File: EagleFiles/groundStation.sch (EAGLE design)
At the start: 23 parts, among them IC1 TP4056

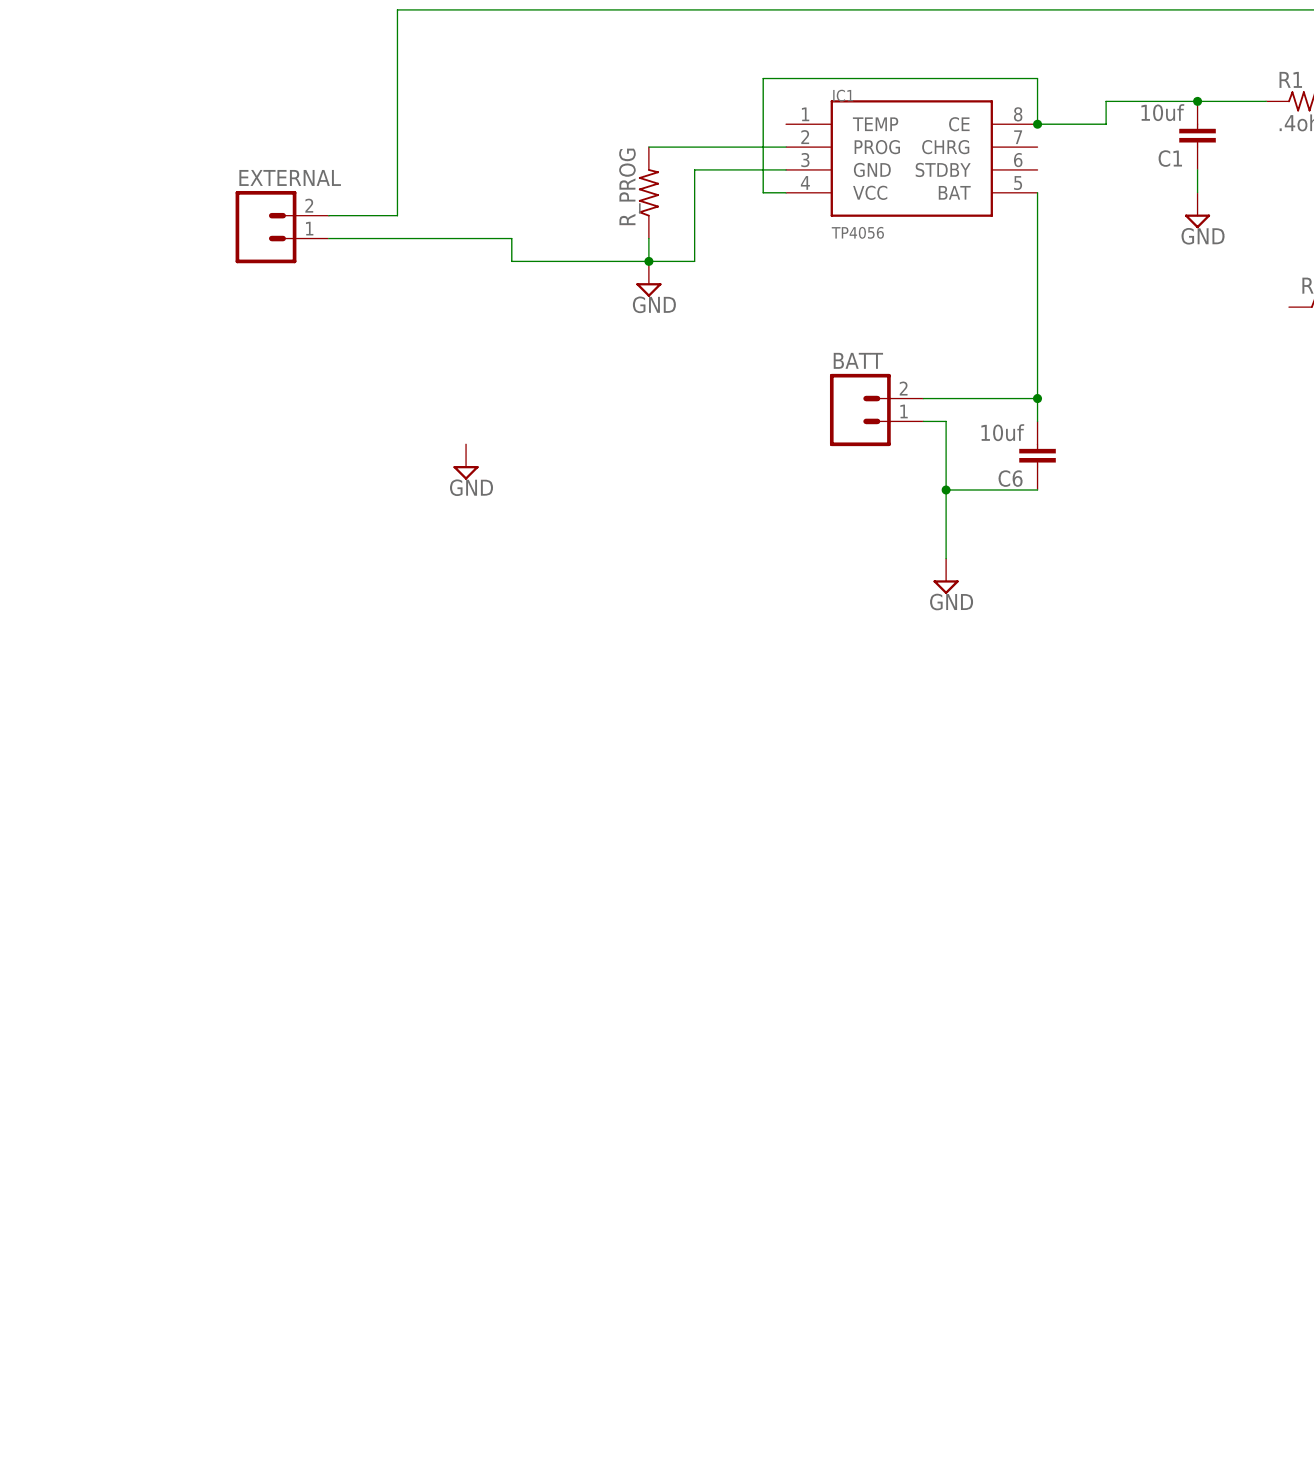
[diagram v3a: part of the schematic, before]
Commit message: added uass ground station
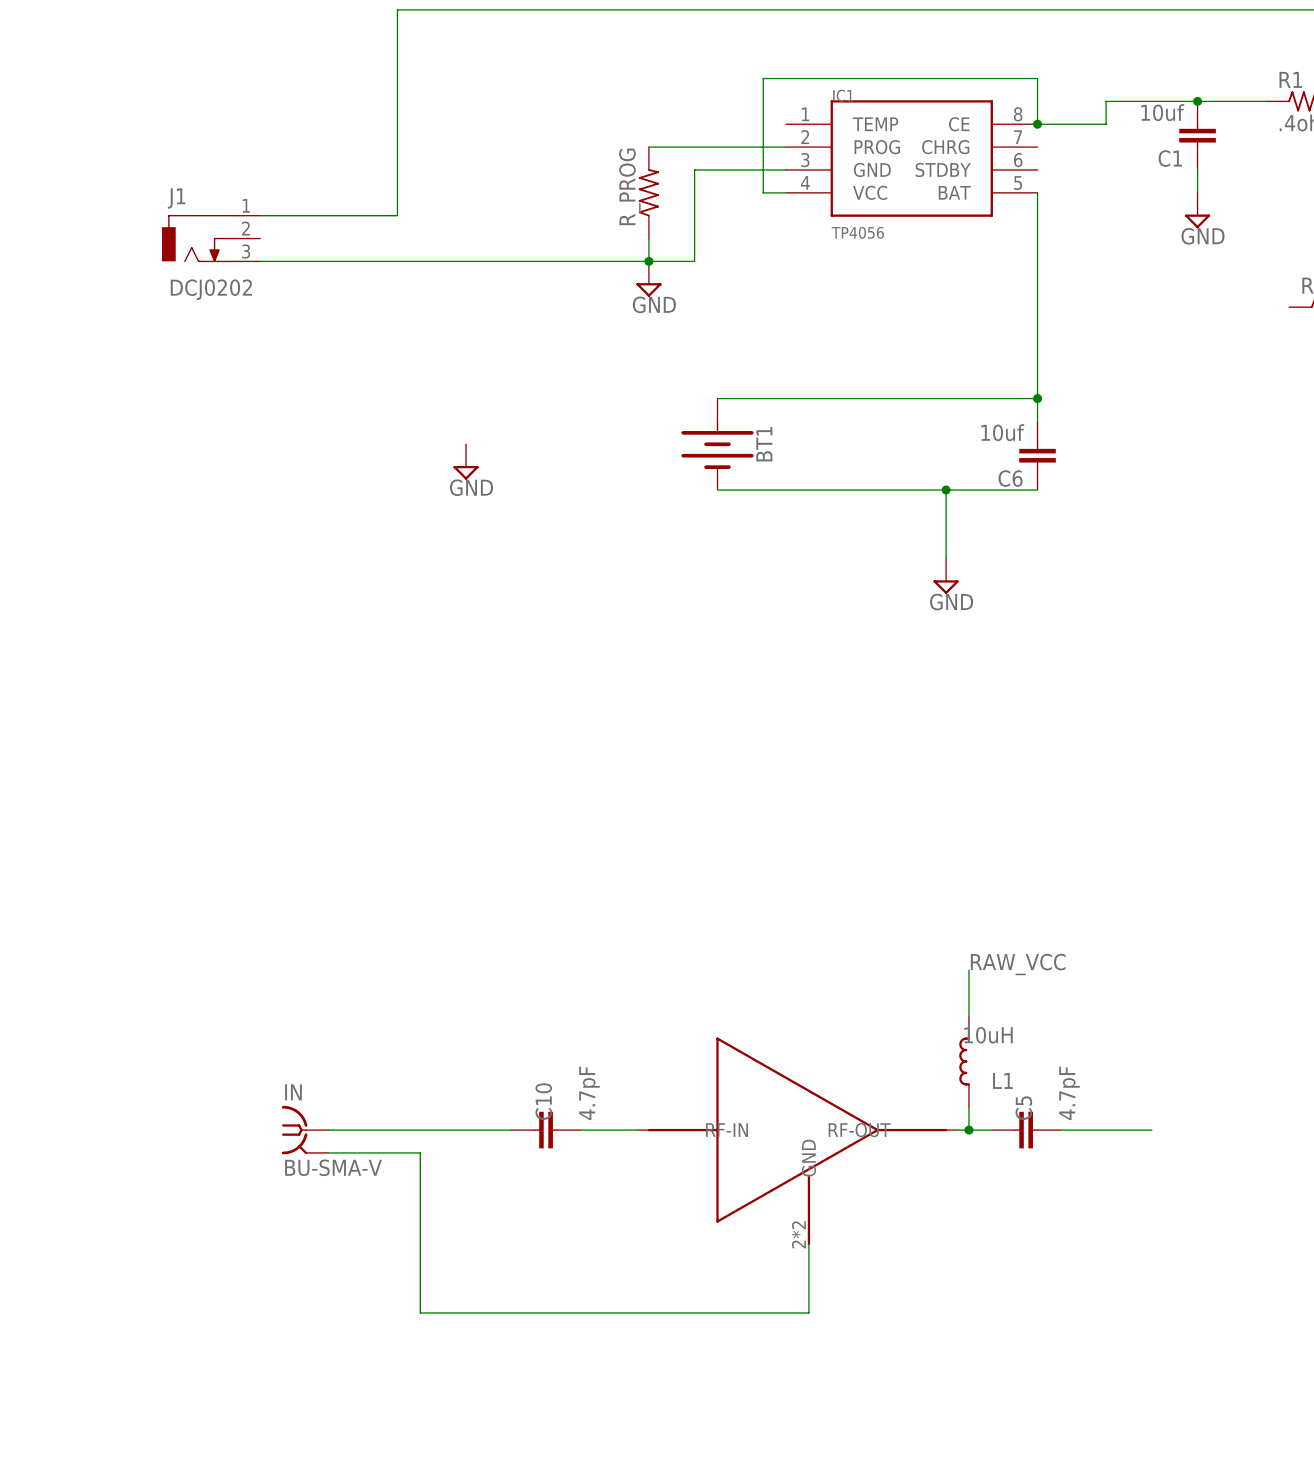
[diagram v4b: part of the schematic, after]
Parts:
- removed BATT, EXTERNAL: (no value), con-amp-quick:M02
- added BT1: (no value), SparkFun-Batteries:BATTERY-18650
- added C10, C5: 4.7pF, SparkFun-Capacitors:10UF-0603-6.3V-20%
- added IN: BU-SMA-V, con-coax:BU-SMA-V
- added J1: DCJ0202, con-jack:DCJ0202
- added L1: 10uH, rc-master-smd:L_0603
- added U$5: PSA4-5043+, PSA4-5043_:PSA4-5043+
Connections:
- new net GND3: IN.2, U$5.GND
- new net N$23: C5.2
- new net N$24: C10.1, IN.1
- new net N$25: C10.2, U$5.RF-IN
- new net N$26: C5.1, L1.2, U$5.RF-OUT
- net GND: now also BT1.-, J1.3; no longer BATT.1, EXTERNAL.1
- net N$1: now also BT1.+; no longer BATT.2
- net RAW_VCC: now also J1.1, L1.1; no longer EXTERNAL.2
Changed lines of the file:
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@@
 <part name="U$3" library="RFFM6406" deviceset="RFFM6404" device=""/>
 <part name="IC1" library="TP4056" deviceset="TP4056" device=""/>
-<part name="BATT" library="con-amp-quick" library_urn="urn:adsk.eagle:library:125" deviceset="M02" device="" package3d_urn="urn:adsk.eagle:package:5956/1"/>
 <part name="SUPPLY1" library="supply2" library_urn="urn:adsk.eagle:library:372" deviceset="GND" device=""/>
 <part name="R_PROG" library="adafruit" library_urn="urn:adsk.eagle:library:420" deviceset="R-US_" device="R0603" package3d_urn="urn:adsk.eagle:package:6240565/1"/>
@@
 <part name="C4" library="SparkFun-Capacitors" deviceset="0.1UF" device="-0603-100V-10%" value="1uf"/>
 <part name="R8" library="adafruit" library_urn="urn:adsk.eagle:library:420" deviceset="R-US_" device="R0603" package3d_urn="urn:adsk.eagle:package:6240565/1" value="50ohm"/>
-<part name="EXTERNAL" library="con-amp-quick" library_urn="urn:adsk.eagle:library:125" deviceset="M02" device="" package3d_urn="urn:adsk.eagle:package:5956/1"/>
+<part name="BT1" library="SparkFun-Batteries" library_urn="urn:adsk.eagle:library:508" deviceset="BATTERY" device="-18650" package3d_urn="urn:adsk.eagle:package:37227/1"/>
+<part name="J1" library="con-jack" library_urn="urn:adsk.eagle:library:154" deviceset="DCJ0202" device="" package3d_urn="urn:adsk.eagle:package:7491/1"/>
+<part name="U$5" library="PSA4-5043_" deviceset="PSA4-5043+" device=""/>
+<part name="C5" library="SparkFun-Capacitors" library_urn="urn:adsk.eagle:library:510" deviceset="10UF" device="-0603-6.3V-20%" package3d_urn="urn:adsk.eagle:package:37414/1" value="4.7pF"/>
+<part name="C10" library="SparkFun-Capacitors" library_urn="urn:adsk.eagle:library:510" deviceset="10UF" device="-0603-6.3V-20%" package3d_urn="urn:adsk.eagle:package:37414/1" value="4.7pF"/>
+<part name="L1" library="rc-master-smd" deviceset="L_" device="0603" value="10uH"/>
+<part name="IN" library="con-coax" library_urn="urn:adsk.eagle:library:133" deviceset="BU-SMA-V" device="" package3d_urn="urn:adsk.eagle:package:6211/1"/>
 </parts>
 <sheets>
@@
 <attribute name="VALUE" x="246.38" y="292.1" size="1.27" layer="96"/>
 </instance>
-<instance part="BATT" gate="G$1" x="248.92" y="271.78" smashed="yes">
-<attribute name="VALUE" x="246.38" y="266.7" size="1.778" layer="96"/>
-<attribute name="NAME" x="246.38" y="277.622" size="1.778" layer="95"/>
-</instance>
 <instance part="SUPPLY1" gate="GND" x="259.08" y="254" smashed="yes">
 <attribute name="VALUE" x="257.175" y="250.825" size="1.778" layer="96"/>
@@
 <attribute name="VALUE" x="46.482" y="242.57" size="1.778" layer="96" rot="R90"/>
 </instance>
-<instance part="EXTERNAL" gate="G$1" x="182.88" y="292.1" smashed="yes">
-<attribute name="VALUE" x="180.34" y="287.02" size="1.778" layer="96"/>
-<attribute name="NAME" x="180.34" y="297.942" size="1.778" layer="95"/>
+<instance part="BT1" gate="G$1" x="233.68" y="269.24" smashed="yes" rot="R270">
+<attribute name="NAME" x="237.998" y="269.24" size="1.778" layer="95" font="vector" rot="R270" align="bottom-center"/>
+<attribute name="VALUE" x="229.362" y="269.24" size="1.778" layer="96" font="vector" rot="R270" align="top-center"/>
+</instance>
+<instance part="J1" gate="G$1" x="175.26" y="292.1" smashed="yes">
+<attribute name="NAME" x="172.72" y="295.91" size="1.778" layer="95"/>
+<attribute name="VALUE" x="172.72" y="285.75" size="1.778" layer="96"/>
+</instance>
+<instance part="U$5" gate="G$1" x="241.3" y="193.04" smashed="yes"/>
+<instance part="C5" gate="G$1" x="269.24" y="193.04" smashed="yes" rot="R90">
+<attribute name="NAME" x="268.605" y="194.056" size="1.778" layer="95" rot="R90"/>
+<attribute name="VALUE" x="273.431" y="194.056" size="1.778" layer="96" rot="R90"/>
+</instance>
+<instance part="C10" gate="G$1" x="215.9" y="193.04" smashed="yes" rot="R90">
+<attribute name="NAME" x="215.265" y="194.056" size="1.778" layer="95" rot="R90"/>
+<attribute name="VALUE" x="220.091" y="194.056" size="1.778" layer="96" rot="R90"/>
+</instance>
+<instance part="L1" gate="G$1" x="261.62" y="200.66" smashed="yes" rot="R90">
+<attribute name="NAME" x="266.7" y="199.39" size="1.778" layer="95" rot="R180"/>
+<attribute name="VALUE" x="266.7" y="204.47" size="1.778" layer="96" rot="R180"/>
+</instance>
+<instance part="IN" gate="G$1" x="187.96" y="193.04" smashed="yes">
+<attribute name="VALUE" x="185.42" y="187.96" size="1.778" layer="96"/>
+<attribute name="NAME" x="185.42" y="196.342" size="1.778" layer="95"/>
 </instance>
 </instances>
@@
 </segment>
 <segment>
-<pinref part="BATT" gate="G$1" pin="1"/>
 <pinref part="SUPPLY1" gate="GND" pin="GND"/>
-<wire x1="256.54" y1="271.78" x2="259.08" y2="271.78" width="0.1524" layer="91"/>
-<wire x1="259.08" y1="271.78" x2="259.08" y2="264.16" width="0.1524" layer="91"/>
 <pinref part="C6" gate="G$1" pin="1"/>
 <wire x1="259.08" y1="264.16" x2="259.08" y2="256.54" width="0.1524" layer="91"/>
 <wire x1="269.24" y1="264.16" x2="259.08" y2="264.16" width="0.1524" layer="91"/>
+<pinref part="BT1" gate="G$1" pin="-"/>
+<wire x1="259.08" y1="264.16" x2="233.68" y2="264.16" width="0.1524" layer="91"/>
 <junction x="259.08" y="264.16"/>
 </segment>
@@
 <wire x1="231.14" y1="289.56" x2="226.06" y2="289.56" width="0.1524" layer="91"/>
 <junction x="226.06" y="289.56"/>
-<pinref part="EXTERNAL" gate="G$1" pin="1"/>
-<wire x1="190.5" y1="292.1" x2="210.82" y2="292.1" width="0.1524" layer="91"/>
-<wire x1="210.82" y1="292.1" x2="210.82" y2="289.56" width="0.1524" layer="91"/>
-<wire x1="210.82" y1="289.56" x2="226.06" y2="289.56" width="0.1524" layer="91"/>
+<pinref part="J1" gate="G$1" pin="3"/>
+<wire x1="226.06" y1="289.56" x2="182.88" y2="289.56" width="0.1524" layer="91"/>
 </segment>
 <segment>
@@
 <net name="N$1" class="0">
 <segment>
-<pinref part="BATT" gate="G$1" pin="2"/>
 <pinref part="IC1" gate="G$1" pin="BAT"/>
-<wire x1="256.54" y1="274.32" x2="269.24" y2="274.32" width="0.1524" layer="91"/>
+<wire x1="269.24" y1="271.78" x2="269.24" y2="274.32" width="0.1524" layer="91"/>
+<pinref part="C6" gate="G$1" pin="2"/>
+<pinref part="BT1" gate="G$1" pin="+"/>
 <wire x1="269.24" y1="274.32" x2="269.24" y2="297.18" width="0.1524" layer="91"/>
-<pinref part="C6" gate="G$1" pin="2"/>
-<wire x1="269.24" y1="271.78" x2="269.24" y2="274.32" width="0.1524" layer="91"/>
+<wire x1="233.68" y1="274.32" x2="269.24" y2="274.32" width="0.1524" layer="91"/>
 <junction x="269.24" y="274.32"/>
 </segment>
@@
 <wire x1="304.8" y1="307.34" x2="309.88" y2="307.34" width="0.1524" layer="91"/>
 <label x="309.88" y="307.34" size="1.778" layer="95"/>
-<pinref part="EXTERNAL" gate="G$1" pin="2"/>
-<wire x1="190.5" y1="294.64" x2="198.12" y2="294.64" width="0.1524" layer="91"/>
 <wire x1="198.12" y1="294.64" x2="198.12" y2="317.5" width="0.1524" layer="91"/>
 <wire x1="198.12" y1="317.5" x2="304.8" y2="317.5" width="0.1524" layer="91"/>
 <wire x1="304.8" y1="317.5" x2="304.8" y2="307.34" width="0.1524" layer="91"/>
 <junction x="304.8" y="307.34"/>
+<pinref part="J1" gate="G$1" pin="1"/>
+<wire x1="182.88" y1="294.64" x2="198.12" y2="294.64" width="0.1524" layer="91"/>
 </segment>
 <segment>
@@
 <wire x1="0" y1="35.56" x2="-15.24" y2="35.56" width="0.1524" layer="91"/>
 <label x="-12.7" y="35.56" size="1.778" layer="95"/>
+</segment>
+<segment>
+<pinref part="L1" gate="G$1" pin="1"/>
+<wire x1="261.62" y1="205.74" x2="261.62" y2="210.82" width="0.1524" layer="91"/>
+<label x="261.62" y="210.82" size="1.778" layer="95"/>
 </segment>
 </net>
@@
 </segment>
 </net>
+<net name="N$23" class="0">
+<segment>
+<pinref part="C5" gate="G$1" pin="2"/>
+<wire x1="271.78" y1="193.04" x2="281.94" y2="193.04" width="0.1524" layer="91"/>
+</segment>
+</net>
+<net name="N$24" class="0">
+<segment>
+<pinref part="C10" gate="G$1" pin="1"/>
+<pinref part="IN" gate="G$1" pin="1"/>
+<wire x1="210.82" y1="193.04" x2="190.5" y2="193.04" width="0.1524" layer="91"/>
+</segment>
+</net>
+<net name="N$25" class="0">
+<segment>
+<pinref part="C10" gate="G$1" pin="2"/>
+<pinref part="U$5" gate="G$1" pin="RF-IN"/>
+<wire x1="218.44" y1="193.04" x2="224.79" y2="193.04" width="0.1524" layer="91"/>
+</segment>
+</net>
+<net name="N$26" class="0">
+<segment>
+<pinref part="U$5" gate="G$1" pin="RF-OUT"/>
+<pinref part="C5" gate="G$1" pin="1"/>
+<wire x1="260.35" y1="193.04" x2="261.62" y2="193.04" width="0.1524" layer="91"/>
+<pinref part="L1" gate="G$1" pin="2"/>
+<wire x1="261.62" y1="193.04" x2="264.16" y2="193.04" width="0.1524" layer="91"/>
+<wire x1="261.62" y1="195.58" x2="261.62" y2="193.04" width="0.1524" layer="91"/>
+<junction x="261.62" y="193.04"/>
+</segment>
+</net>
+<net name="GND3" class="0">
+<segment>
+<pinref part="U$5" gate="G$1" pin="GND"/>
+<wire x1="243.84" y1="180.34" x2="243.84" y2="172.72" width="0.1524" layer="91"/>
+<wire x1="200.66" y1="172.72" x2="243.84" y2="172.72" width="0.1524" layer="91"/>
+<pinref part="IN" gate="G$1" pin="2"/>
+<wire x1="190.5" y1="190.5" x2="200.66" y2="190.5" width="0.1524" layer="91"/>
+<wire x1="200.66" y1="190.5" x2="200.66" y2="172.72" width="0.1524" layer="91"/>
+</segment>
+</net>
